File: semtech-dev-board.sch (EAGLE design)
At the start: 21 parts, among them Q1 OPTIONAL, Q2 BSS123, Q3 BSS84, U1 MIC5219 3.3V, X1 BU-SMA-G, X2 BU-SMA-G, X3 BU-SMA-G, X4 BU-SMA-G, X5 BU-SMA-G

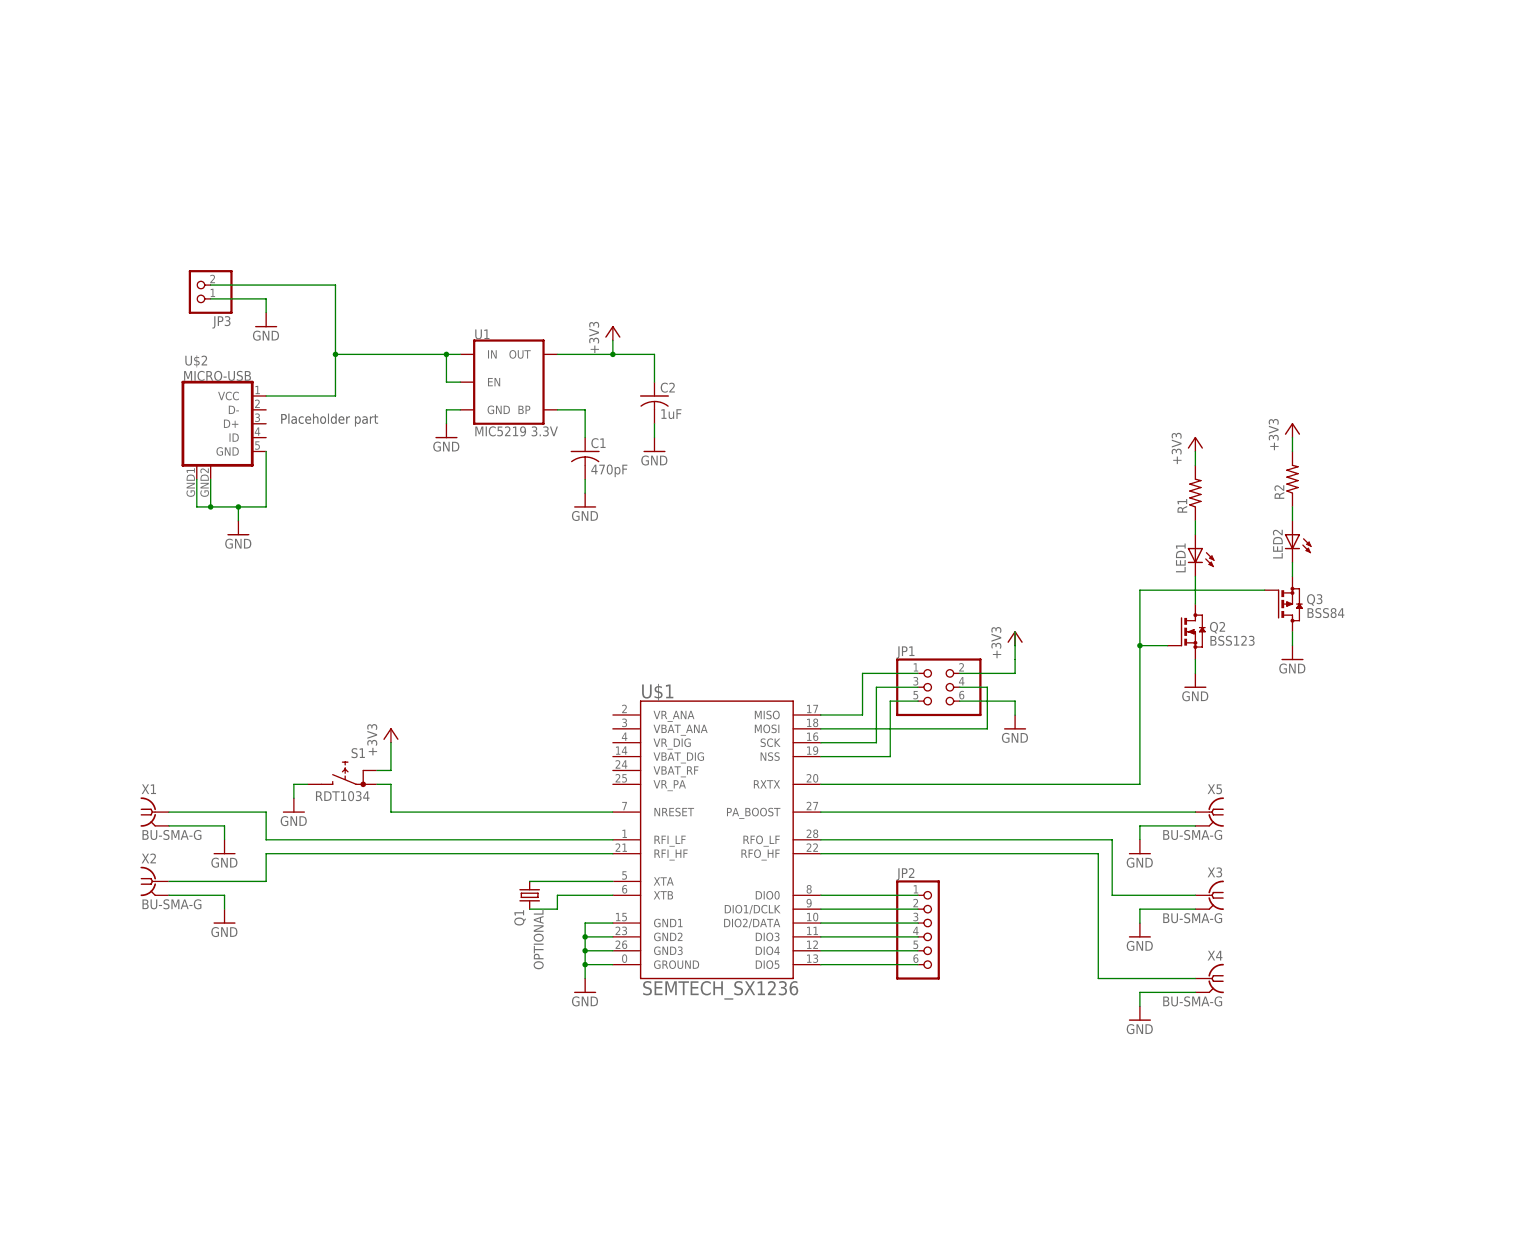
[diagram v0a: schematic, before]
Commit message: Connected power supply
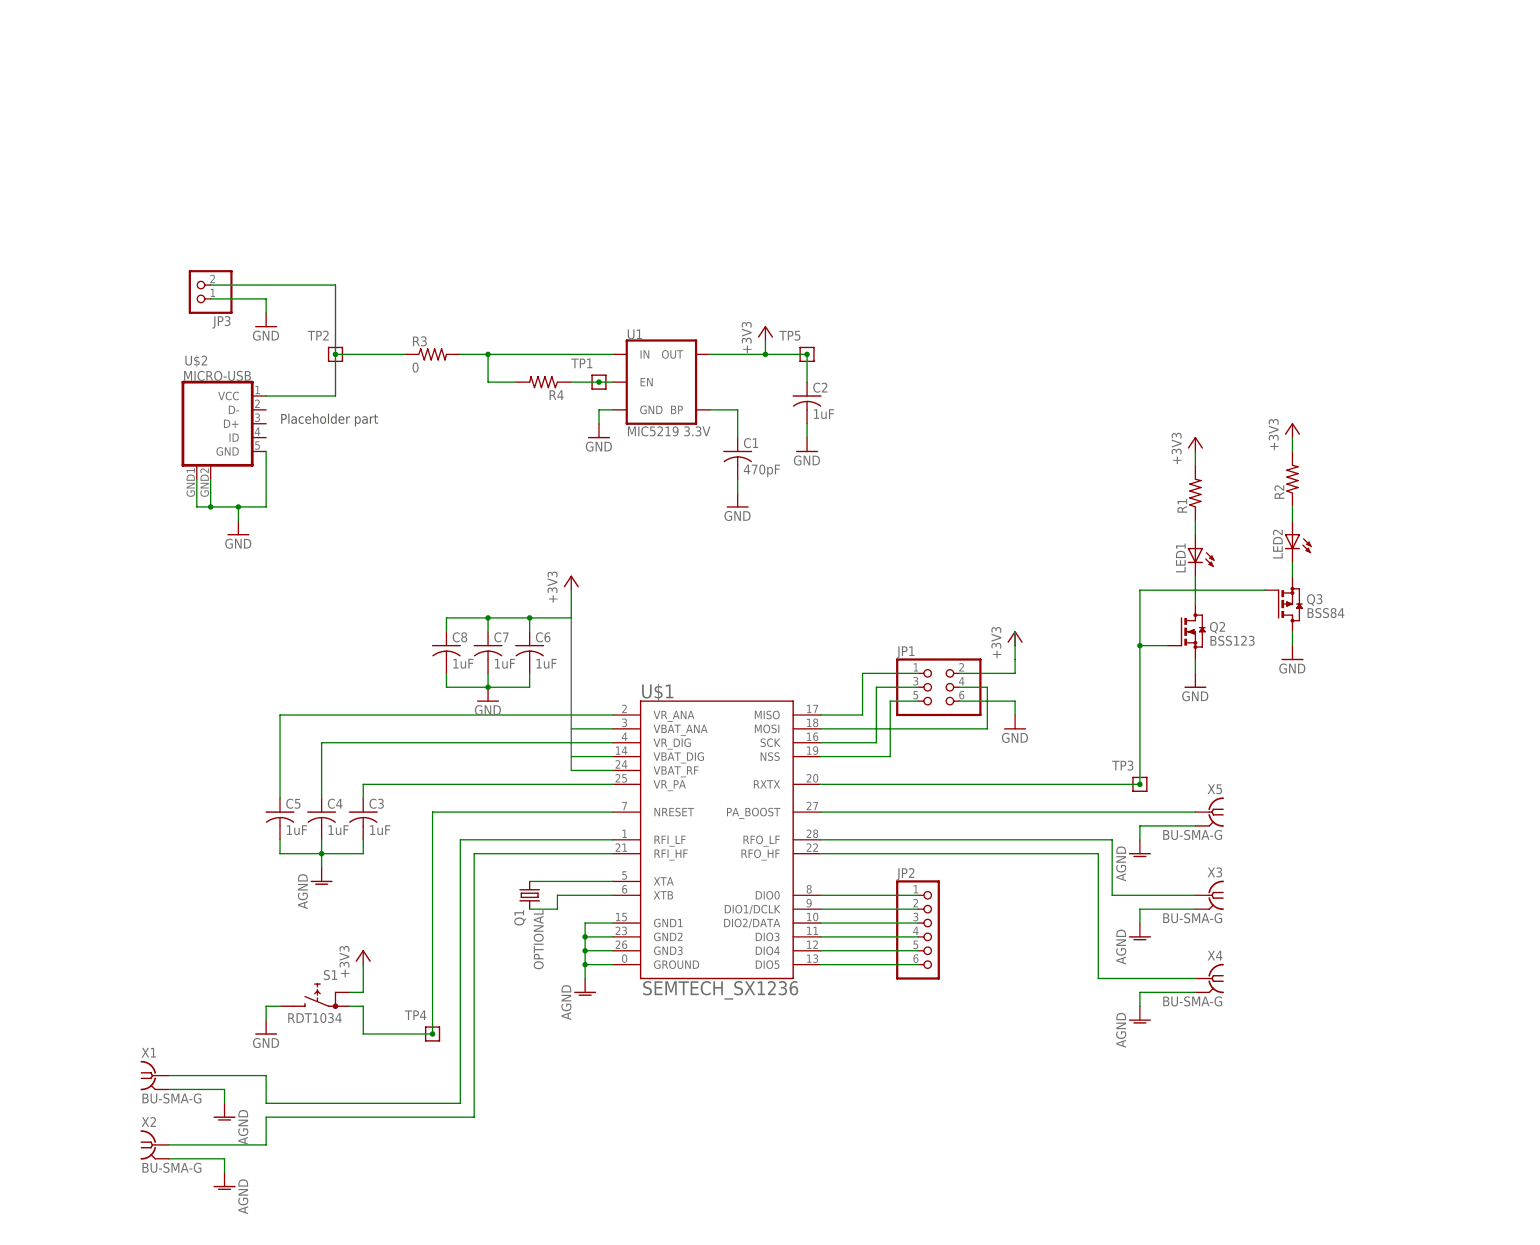
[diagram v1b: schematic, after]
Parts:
- added C3, C4, C5, C6, C7, C8: 1uF, rcl:C-USC0805
- added R3: 0, rcl:R-US_R0805
- added R4: (no value), rcl:R-US_R0805
- added TP1, TP2, TP3, TP4, TP5: TEST-POINT, low-gain-radio:TEST-POINT
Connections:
- new net AGND: C3.2, C4.2, C5.2, U$1.GND1, U$1.GND2, U$1.GND3, U$1.GROUND, X1.2, X2.2, X3.2, X4.2, X5.2
- new net N$26: R4.1, TP1.1, U1.EN
- new net N$27: R3.2, R4.2, U1.IN
- new net N$28: C4.1, U$1.VR_DIG
- new net N$29: C3.1, U$1.VR_PA
- new net N$30: C5.1, U$1.VR_ANA
- net +3V3: now also C6.1, C7.1, C8.1, TP5.1, U$1.VBAT_ANA, U$1.VBAT_DIG, U$1.VBAT_RF
- net GND: now also C6.2, C7.2, C8.2; no longer U$1.GND1, U$1.GND2, U$1.GND3, U$1.GROUND, X1.2, X2.2, X3.2, X4.2, X5.2
- net N$18: now also R3.1, TP2.1; no longer U1.EN, U1.IN
- net N$24: now also TP3.1
- net N$25: now also TP4.1
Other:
- moved on the sheet: C1, C2, S1, U1, X1, X2

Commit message: named nets
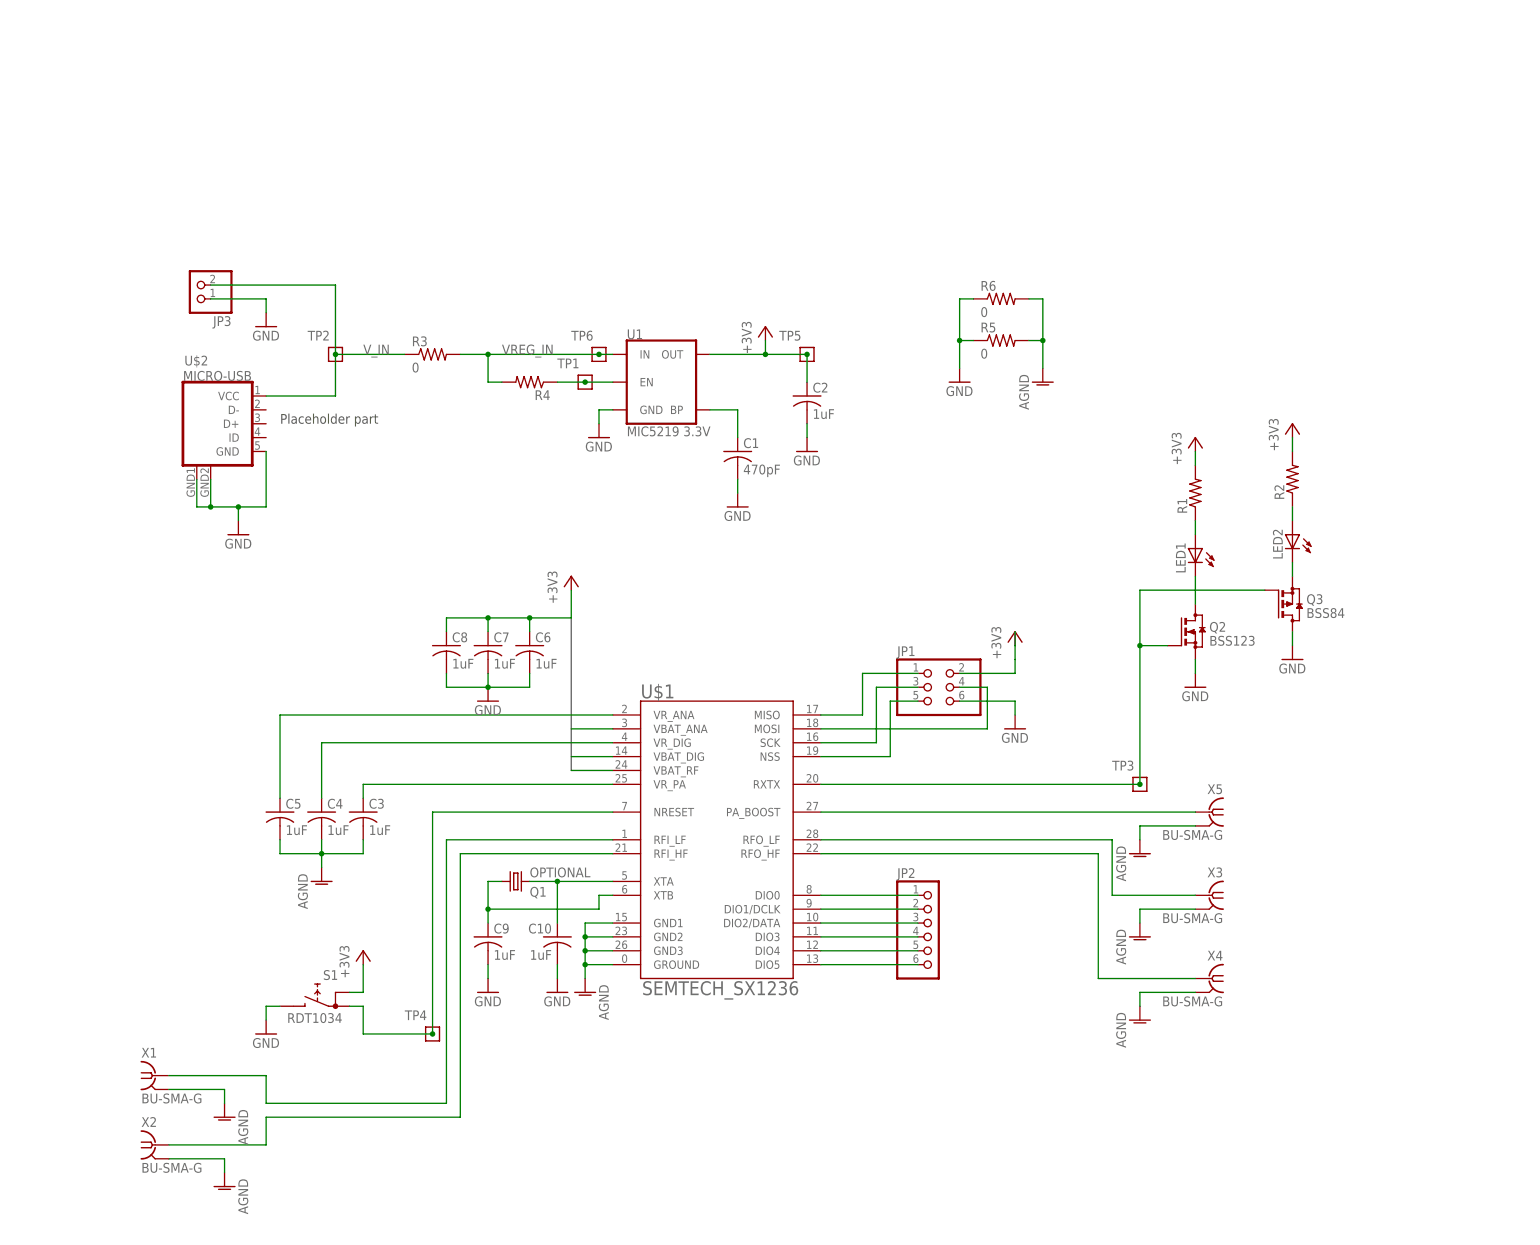
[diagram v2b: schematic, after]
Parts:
- added C10, C9: 1uF, rcl:C-USC0805
- added R5, R6: 0, rcl:R-US_R0805
- added TP6: TEST-POINT, low-gain-radio:TEST-POINT
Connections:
- net N$10 renamed DIO2
- net N$11 renamed DIO3
- net N$12 renamed DIO4
- net N$13 renamed DIO5
- net N$14 renamed RFI_HF
- net N$15 renamed RFI_LF
- net N$16 renamed RFO_HF
- net N$17 renamed RFO_LF
- net N$18 renamed V_IN
- net N$19 renamed BP
- net N$2 renamed SPI_NSS
- net N$21 renamed PA_BOOST
- net N$24 renamed RXTX
- net N$25 renamed SX1236_RST
- net N$26 renamed 5219_EN
- net N$3 renamed SPI_SCK
- net N$4 renamed SPI_MISO
- net N$5 renamed SPI_MOSI
- net N$8 renamed DIO0
- net N$9 renamed DIO1
- removed net N$22: Q1.1, U$1.XTA
- removed net N$23: Q1.2, U$1.XTB
- removed net N$27: R3.2, R4.2, U1.IN
- new net N$2: C10.1, Q1.2, U$1.XTA
- new net VREG_IN: R3.2, R4.2, TP6.1, U1.IN
- new net XTALB: C9.1, Q1.1, U$1.XTB
- net AGND: now also R5.2, R6.2
- net GND: now also C10.2, C9.2, R5.1, R6.1
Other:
- moved on the sheet: Q1, R4, TP1

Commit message: Fixed bus
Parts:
- added R7: 0, rcl:R-US_R0805
- C10, C9: value 1uF -> 6pF
- C3, C4, C5, C6, C7, C8: value 1uF -> 100nF
- Q1: value OPTIONAL -> (none)
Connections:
- net N$28 renamed VR_DIG
- net N$29 renamed VR_PA
- net N$30 renamed VR_ANA
- new net VBAT: C6.1, C7.1, C8.1, R7.1, U$1.VBAT_ANA
- net +3V3: now also R7.2; no longer C6.1, C7.1, C8.1, U$1.VBAT_ANA
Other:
- note added: "OPTIONAL"
- note added: "SUPPLY"
- moved on the sheet: C10, C3, C5, C6, C7, C8, C9, LED2, Q1, Q3, R2, R5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

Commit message: adjustments based on Friday meeting
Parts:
- added R8: 1k, rcl:R-US_R0805
- JP1: device pinhead:PINHD-2X3 -> pinhead:PINHD-1X4
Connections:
- net SPI_MISO renamed N$3
- new net N$4: R8.1, S1.A
- net +3V3: now also R8.2; no longer JP1.2, S1.A
- net GND: no longer JP1.6
- net SPI_MOSI: now also JP1.2; no longer JP1.4
- net SPI_NSS: now also JP1.4; no longer JP1.5
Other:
- moved on the sheet: C6, C7, C8, R7

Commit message: Updates from Sunday meeting
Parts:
- removed X5: BU-SMA-G, con-coax:BU-SMA-G
- added TP7: TEST-POINT, low-gain-radio:TEST-POINT
- JP2: device pinhead:PINHD-1X6 -> pinhead:PINHD-1X7
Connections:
- removed net DIO0: JP2.1, U$1.DIO0
- removed net DIO1: JP2.2, U$1.DIO1/DCLK
- removed net DIO2: JP2.3, U$1.DIO2/DATA
- removed net DIO3: JP2.4, U$1.DIO3
- removed net DIO4: JP2.5, U$1.DIO4
- removed net DIO5: JP2.6, U$1.DIO5
- new net N$10: JP2.4, U$1.DIO2/DATA
- new net N$11: JP2.5, U$1.DIO3
- new net N$12: JP2.6, U$1.DIO4
- new net N$13: JP2.7, U$1.DIO5
- new net N$5: JP2.2, U$1.DIO0
- new net N$9: JP2.3, U$1.DIO1/DCLK
- net AGND: no longer X5.2
- net PA_BOOST: now also TP7.1; no longer X5.1
- net RXTX: now also JP2.1
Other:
- moved on the sheet: C3, C4, C5, C6, C7, C8, LED1, LED2, Q2, Q3, R1, R2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
